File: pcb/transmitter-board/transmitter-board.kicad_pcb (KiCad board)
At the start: 2 copper layers, 28.9 x 20.5 mm, 28 parts, among them J1 USB-C_USB-310F-B-SU, Q3 AO3400A, Q4 AO3400A, SW1 SW_DPDT_x2, U1 NE555D, U3 TP4056-42-ESOP8, U4 DW01A

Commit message: Move USB
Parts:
- moved J1 1.05 mm to (161.3, 119.4)
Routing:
- net +3V8: track 35.4 -> 39.1 mm
- net GND: track 39.5 -> 38.1 mm
- net /IN+: track 41.0 -> 42.2 mm
- net Net-(J1-CC1): track 13.9 -> 12.7 mm
- net Net-(J1-CC2): track 6.40 -> 7.45 mm
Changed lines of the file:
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@@
 	(footprint "DW-footprints:USB-C-Receptacle_USB-310-B-SU"
 		(layer "F.Cu")
-		(at 161.33 118.375)
+		(at 161.33 119.425)
 		(descr "3A 1 Surface Mount, Right Angle 16P Female Type-C SMD USB Connectors ROHS")
 		(tags "USB, CONNECTOR, SMD")
@@
 	)
 	(segment
-		(start 157.585 114.695)
-		(end 157.01 115.27)
-		(width 0.2)
-		(layer "F.Cu")
-		(net 2)
-	)
-	(segment
 		(start 165.944222 113.237753)
 		(end 165.944222 112.854742)
@@
 	)
 	(segment
-		(start 158.13 114.695)
-		(end 157.585 114.695)
-		(width 0.2)
-		(layer "F.Cu")
-		(net 2)
-	)
-	(segment
 		(start 166.989903 110.181374)
 		(end 166.989903 111.659946)
@@
 	)
 	(segment
-		(start 163.73 114.695)
-		(end 163.73 115.083112)
+		(start 159.95 117.35)
+		(end 162.7 117.35)
 		(width 0.2)
 		(layer "F.Cu")
@@
 	)
 	(segment
-		(start 159.35 115.7)
-		(end 158.93 115.28)
+		(start 158.9 115.02)
+		(end 158.9 115.594999)
+		(width 0.2)
+		(layer "F.Cu")
+		(net 4)
+	)
+	(segment
+		(start 158.93 116.33)
+		(end 159.95 117.35)
 		(width 0.2)
 		(layer "F.Cu")
@@
 	)
 	(segment
-		(start 163.73 114.695)
-		(end 163.73 115.22)
+		(start 158.93 115.745)
+		(end 158.93 116.33)
 		(width 0.2)
 		(layer "F.Cu")
@@
 	)
 	(segment
-		(start 163.113112 115.7)
-		(end 159.35 115.7)
+		(start 163.4 116.683992)
+		(end 163.73 116.353992)
+		(width 0.2)
+		(layer "F.Cu")
+		(net 4)
+	)
+	(segment
+		(start 163.73 116.353992)
+		(end 163.73 115.745)
+		(width 0.2)
+		(layer "F.Cu")
+		(net 4)
+	)
+	(segment
+		(start 162.7 117.35)
+		(end 163.366008 116.683992)
 		(width 0.2)
 		(layer "F.Cu")
@@
 	)
 	(segment
-		(start 163.73 115.083112)
-		(end 163.113112 115.7)
-		(width 0.2)
+		(start 166.339634 109.22)
+		(end 165.727866 108.608232)
+		(width 0.3)
 		(layer "F.Cu")
 		(net 4)
 	)
 	(segment
-		(start 166.339634 109.22)
-		(end 165.727866 108.608232)
-		(width 0.3)
+		(start 163.366008 116.683992)
+		(end 163.4 116.683992)
+		(width 0.2)
 		(layer "F.Cu")
 		(net 4)
@@
 	)
 	(segment
+		(start 158.35 119.55)
+		(end 157.2 118.4)
+		(width 0.2)
+		(layer "B.Cu")
+		(net 6)
+	)
+	(segment
+		(start 150.772512 118.1)
+		(end 150.001364 117.328852)
+		(width 0.2)
+		(layer "B.Cu")
+		(net 6)
+	)
+	(segment
 		(start 165.73785 110.188892)
 		(end 166.610147 109.316594)
@@
 	)
 	(segment
-		(start 150.514534 116.815682)
-		(end 161.534318 116.815682)
+		(start 162.75 118.9)
+		(end 162.1 119.55)
 		(width 0.2)
 		(layer "B.Cu")
@@
 	)
 	(segment
-		(start 165.73785 112.61215)
-		(end 165.73785 110.188892)
+		(start 155.2 118.1)
+		(end 150.772512 118.1)
+		(width 0.2)
+		(layer "B.Cu")
+		(net 6)
+	)
+	(segment
+		(start 157.2 118.4)
+		(end 155.5 118.4)
+		(width 0.2)
+		(layer "B.Cu")
+		(net 6)
+	)
+	(segment
+		(start 155.5 118.4)
+		(end 155.2 118.1)
 		(width 0.2)
 		(layer "B.Cu")
@@
 	)
 	(segment
-		(start 150.001364 117.328852)
-		(end 150.514534 116.815682)
+		(start 162.75 116.65)
+		(end 162.75 118.9)
 		(width 0.2)
 		(layer "B.Cu")
@@
 	)
 	(segment
-		(start 161.534318 116.815682)
-		(end 165.73785 112.61215)
+		(start 162.1 119.55)
+		(end 158.35 119.55)
+		(width 0.2)
+		(layer "B.Cu")
+		(net 6)
+	)
+	(segment
+		(start 165.73785 110.188892)
+		(end 165.73785 113.66215)
+		(width 0.2)
+		(layer "B.Cu")
+		(net 6)
+	)
+	(segment
+		(start 165.73785 113.66215)
+		(end 162.75 116.65)
 		(width 0.2)
 		(layer "B.Cu")
@@
 	)
 	(segment
-		(start 166.156679 113.75)
-		(end 167.647066 115.240387)
+		(start 163.08 114.120001)
+		(end 163.08 115.745)
 		(width 0.15)
 		(layer "F.Cu")
@@
 	)
 	(segment
-		(start 163.08 114.695)
-		(end 163.08 114.120001)
+		(start 167.647066 115.240387)
+		(end 166.156679 113.75)
 		(width 0.15)
 		(layer "F.Cu")
@@
 	)
 	(segment
-		(start 167.647066 115.240387)
-		(end 167.647066 115.727887)
+		(start 166.156679 113.75)
+		(end 163.450001 113.75)
 		(width 0.15)
 		(layer "F.Cu")
@@
 	(segment
 		(start 163.450001 113.75)
-		(end 166.156679 113.75)
+		(end 163.08 114.120001)
 		(width 0.15)
 		(layer "F.Cu")
@@
 	)
 	(segment
-		(start 163.08 114.120001)
-		(end 163.450001 113.75)
+		(start 167.647066 115.727887)
+		(end 167.647066 115.240387)
 		(width 0.15)
 		(layer "F.Cu")
@@
 	)
 	(segment
+		(start 168.1 116.7)
+		(end 169.082846 115.717154)
+		(width 0.15)
+		(layer "F.Cu")
+		(net 31)
+	)
+	(segment
+		(start 167.4 117)
+		(end 167.7 116.7)
+		(width 0.15)
+		(layer "F.Cu")
+		(net 31)
+	)
+	(segment
+		(start 161.9 118.15)
+		(end 165.55 118.15)
+		(width 0.15)
+		(layer "F.Cu")
+		(net 31)
+	)
+	(segment
 		(start 169.082846 115.717154)
 		(end 169.439439 115.717154)
@@
 	)
 	(segment
-		(start 160.08 113.77)
-		(end 160.15 113.7)
+		(start 160.08 116.73)
+		(end 160.1 116.75)
 		(width 0.15)
 		(layer "F.Cu")
@@
 	)
 	(segment
-		(start 160.4 116.2)
-		(end 161.2 117)
+		(start 160.1 115.725001)
+		(end 160.08 115.745001)
 		(width 0.15)
 		(layer "F.Cu")
@@
 	)
 	(segment
-		(start 167.4 117)
-		(end 167.7 116.7)
+		(start 167.05 117)
+		(end 167.4 117)
 		(width 0.15)
 		(layer "F.Cu")
@@
 	)
 	(segment
-		(start 167.7 116.7)
-		(end 168.1 116.7)
+		(start 165.55 118.15)
+		(end 166.7 117)
 		(width 0.15)
 		(layer "F.Cu")
@@
 	)
 	(segment
-		(start 161.2 117)
-		(end 167.4 117)
+		(start 166.7 117)
+		(end 167.05 117)
 		(width 0.15)
 		(layer "F.Cu")
@@
 	)
 	(segment
-		(start 168.1 116.7)
-		(end 169.082846 115.717154)
+		(start 160.08 115.745001)
+		(end 160.08 115.52)
 		(width 0.15)
 		(layer "F.Cu")
@@
 	)
 	(segment
-		(start 160.08 114.695001)
-		(end 160.08 113.77)
+		(start 167.7 116.7)
+		(end 168.1 116.7)
+		(width 0.15)
+		(layer "F.Cu")
+		(net 31)
+	)
+	(segment
+		(start 160.08 115.745001)
+		(end 160.08 116.73)
+		(width 0.15)
+		(layer "F.Cu")
+		(net 31)
+	)
+	(segment
+		(start 160.08 115.52)
+		(end 160.1 115.5)
 		(width 0.15)
 		(layer "F.Cu")
@@
 		(net 31)
 	)
+	(segment
+		(start 160.1 116.75)
+		(end 160.15 116.8)
+		(width 0.15)
+		(layer "F.Cu")
+		(net 31)
+	)
 	(via
-		(at 160.4 116.2)
+		(at 160.1 116.75)
 		(size 0.5)
 		(drill 0.3)
@@
 	)
 	(via
-		(at 160.15 113.7)
+		(at 161.9 118.15)
 		(size 0.5)
 		(drill 0.3)
 		(layers "F.Cu" "B.Cu")
-		(free yes)
 		(net 31)
 	)
 	(segment
-		(start 160.15 115.95)
-		(end 160.4 116.2)
+		(start 160.1 116.75)
+		(end 161.5 118.15)
 		(width 0.15)
 		(layer "B.Cu")
@@
 	)
 	(segment
-		(start 160.15 113.7)
-		(end 160.15 115.95)
+		(start 161.5 118.15)
+		(end 161.9 118.15)
 		(width 0.15)
 		(layer "B.Cu")

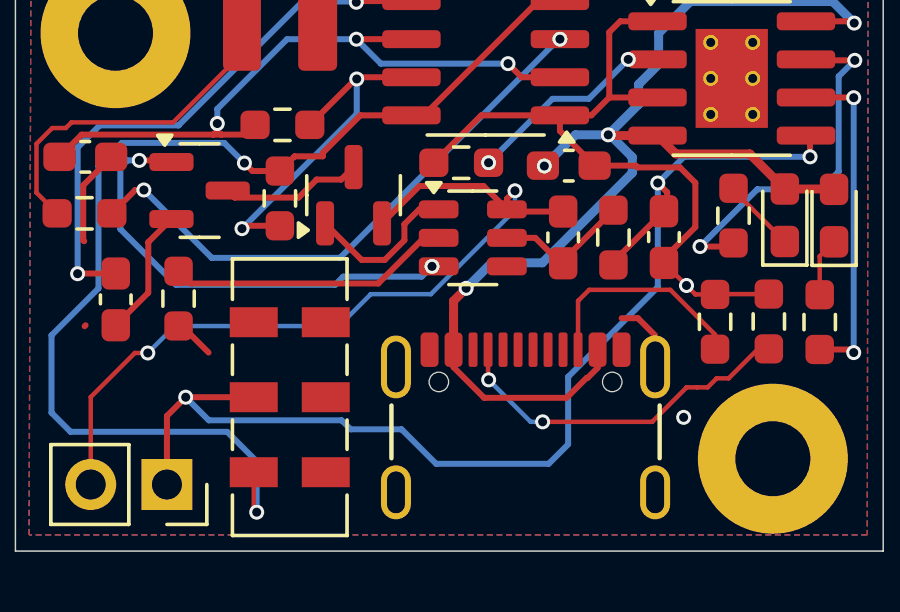
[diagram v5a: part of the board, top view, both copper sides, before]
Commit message: Edited transmitter-board schematic
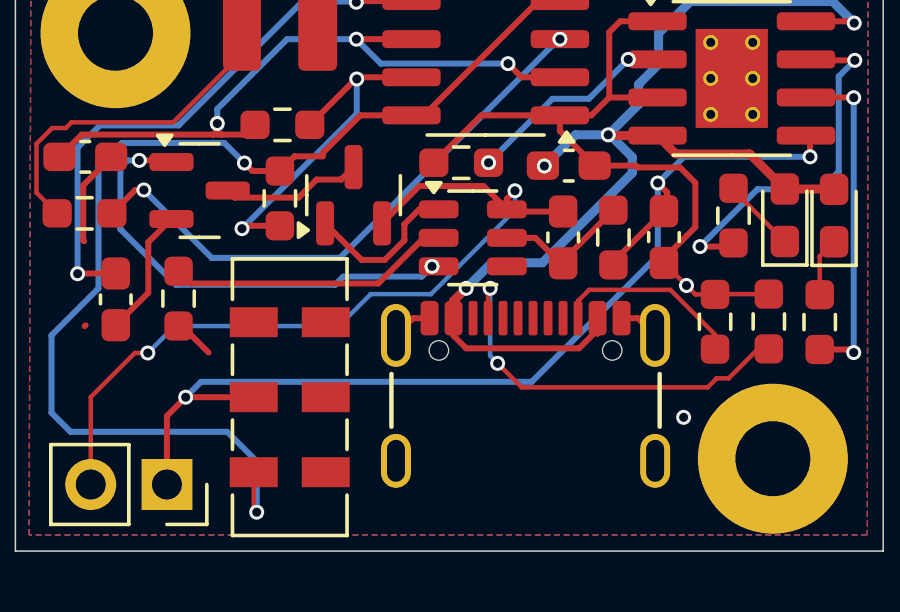
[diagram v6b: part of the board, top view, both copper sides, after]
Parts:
- moved J1 1.05 mm to (161.3, 118.4)
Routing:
- net +3V8: track 39.1 -> 35.4 mm
- net GND: track 38.1 -> 39.5 mm
- net /IN+: track 42.2 -> 41.0 mm
- net Net-(J1-CC1): track 12.7 -> 13.9 mm
- net Net-(J1-CC2): track 7.45 -> 6.40 mm
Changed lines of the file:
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@@
 	(footprint "DW-footprints:USB-C-Receptacle_USB-310-B-SU"
 		(layer "F.Cu")
-		(at 161.33 119.425)
+		(at 161.33 118.375)
 		(descr "3A 1 Surface Mount, Right Angle 16P Female Type-C SMD USB Connectors ROHS")
 		(tags "USB, CONNECTOR, SMD")
@@
 	)
 	(segment
+		(start 157.585 114.695)
+		(end 157.01 115.27)
+		(width 0.2)
+		(layer "F.Cu")
+		(net 2)
+	)
+	(segment
 		(start 165.944222 113.237753)
 		(end 165.944222 112.854742)
@@
 	)
 	(segment
+		(start 158.13 114.695)
+		(end 157.585 114.695)
+		(width 0.2)
+		(layer "F.Cu")
+		(net 2)
+	)
+	(segment
 		(start 166.989903 110.181374)
 		(end 166.989903 111.659946)
@@
 	)
 	(segment
-		(start 159.95 117.35)
-		(end 162.7 117.35)
+		(start 163.73 114.695)
+		(end 163.73 115.083112)
 		(width 0.2)
 		(layer "F.Cu")
@@
 	)
 	(segment
-		(start 158.9 115.02)
-		(end 158.9 115.594999)
-		(width 0.2)
-		(layer "F.Cu")
-		(net 4)
-	)
-	(segment
-		(start 158.93 116.33)
-		(end 159.95 117.35)
+		(start 159.35 115.7)
+		(end 158.93 115.28)
 		(width 0.2)
 		(layer "F.Cu")
@@
 	)
 	(segment
-		(start 158.93 115.745)
-		(end 158.93 116.33)
+		(start 163.73 114.695)
+		(end 163.73 115.22)
 		(width 0.2)
 		(layer "F.Cu")
@@
 	)
 	(segment
-		(start 163.4 116.683992)
-		(end 163.73 116.353992)
-		(width 0.2)
-		(layer "F.Cu")
-		(net 4)
-	)
-	(segment
-		(start 163.73 116.353992)
-		(end 163.73 115.745)
-		(width 0.2)
-		(layer "F.Cu")
-		(net 4)
-	)
-	(segment
-		(start 162.7 117.35)
-		(end 163.366008 116.683992)
+		(start 163.113112 115.7)
+		(end 159.35 115.7)
 		(width 0.2)
 		(layer "F.Cu")
@@
 	)
 	(segment
-		(start 166.339634 109.22)
-		(end 165.727866 108.608232)
-		(width 0.3)
+		(start 163.73 115.083112)
+		(end 163.113112 115.7)
+		(width 0.2)
 		(layer "F.Cu")
 		(net 4)
 	)
 	(segment
-		(start 163.366008 116.683992)
-		(end 163.4 116.683992)
-		(width 0.2)
+		(start 166.339634 109.22)
+		(end 165.727866 108.608232)
+		(width 0.3)
 		(layer "F.Cu")
 		(net 4)
@@
 	)
 	(segment
-		(start 158.35 119.55)
-		(end 157.2 118.4)
-		(width 0.2)
-		(layer "B.Cu")
-		(net 6)
-	)
-	(segment
-		(start 150.772512 118.1)
-		(end 150.001364 117.328852)
-		(width 0.2)
-		(layer "B.Cu")
-		(net 6)
-	)
-	(segment
 		(start 165.73785 110.188892)
 		(end 166.610147 109.316594)
@@
 	)
 	(segment
-		(start 162.75 118.9)
-		(end 162.1 119.55)
+		(start 150.514534 116.815682)
+		(end 161.534318 116.815682)
 		(width 0.2)
 		(layer "B.Cu")
@@
 	)
 	(segment
-		(start 155.2 118.1)
-		(end 150.772512 118.1)
-		(width 0.2)
-		(layer "B.Cu")
-		(net 6)
-	)
-	(segment
-		(start 157.2 118.4)
-		(end 155.5 118.4)
-		(width 0.2)
-		(layer "B.Cu")
-		(net 6)
-	)
-	(segment
-		(start 155.5 118.4)
-		(end 155.2 118.1)
+		(start 165.73785 112.61215)
+		(end 165.73785 110.188892)
 		(width 0.2)
 		(layer "B.Cu")
@@
 	)
 	(segment
-		(start 162.75 116.65)
-		(end 162.75 118.9)
-		(width 0.2)
-		(layer "B.Cu")
-		(net 6)
-	)
-	(segment
-		(start 162.1 119.55)
-		(end 158.35 119.55)
-		(width 0.2)
-		(layer "B.Cu")
-		(net 6)
-	)
-	(segment
-		(start 165.73785 110.188892)
-		(end 165.73785 113.66215)
+		(start 150.001364 117.328852)
+		(end 150.514534 116.815682)
 		(width 0.2)
 		(layer "B.Cu")
@@
 	)
 	(segment
-		(start 165.73785 113.66215)
-		(end 162.75 116.65)
+		(start 161.534318 116.815682)
+		(end 165.73785 112.61215)
 		(width 0.2)
 		(layer "B.Cu")
@@
 	)
 	(segment
-		(start 163.08 114.120001)
-		(end 163.08 115.745)
+		(start 166.156679 113.75)
+		(end 167.647066 115.240387)
 		(width 0.15)
 		(layer "F.Cu")
@@
 	)
 	(segment
-		(start 167.647066 115.240387)
-		(end 166.156679 113.75)
+		(start 163.08 114.695)
+		(end 163.08 114.120001)
 		(width 0.15)
 		(layer "F.Cu")
@@
 	)
 	(segment
-		(start 166.156679 113.75)
-		(end 163.450001 113.75)
+		(start 167.647066 115.240387)
+		(end 167.647066 115.727887)
 		(width 0.15)
 		(layer "F.Cu")
@@
 	(segment
 		(start 163.450001 113.75)
-		(end 163.08 114.120001)
+		(end 166.156679 113.75)
 		(width 0.15)
 		(layer "F.Cu")
@@
 	)
 	(segment
-		(start 167.647066 115.727887)
-		(end 167.647066 115.240387)
+		(start 163.08 114.120001)
+		(end 163.450001 113.75)
 		(width 0.15)
 		(layer "F.Cu")
@@
 	)
 	(segment
-		(start 168.1 116.7)
-		(end 169.082846 115.717154)
-		(width 0.15)
-		(layer "F.Cu")
-		(net 31)
-	)
-	(segment
-		(start 167.4 117)
-		(end 167.7 116.7)
-		(width 0.15)
-		(layer "F.Cu")
-		(net 31)
-	)
-	(segment
-		(start 161.9 118.15)
-		(end 165.55 118.15)
-		(width 0.15)
-		(layer "F.Cu")
-		(net 31)
-	)
-	(segment
 		(start 169.082846 115.717154)
 		(end 169.439439 115.717154)
@@
 	)
 	(segment
-		(start 160.08 116.73)
-		(end 160.1 116.75)
-		(width 0.15)
-		(layer "F.Cu")
-		(net 31)
-	)
-	(segment
-		(start 160.1 115.725001)
-		(end 160.08 115.745001)
-		(width 0.15)
-		(layer "F.Cu")
-		(net 31)
-	)
-	(segment
-		(start 167.05 117)
-		(end 167.4 117)
+		(start 160.08 113.77)
+		(end 160.15 113.7)
 		(width 0.15)
 		(layer "F.Cu")
@@
 	)
 	(segment
-		(start 165.55 118.15)
-		(end 166.7 117)
+		(start 160.4 116.2)
+		(end 161.2 117)
 		(width 0.15)
 		(layer "F.Cu")
@@
 	)
 	(segment
-		(start 166.7 117)
-		(end 167.05 117)
-		(width 0.15)
-		(layer "F.Cu")
-		(net 31)
-	)
-	(segment
-		(start 160.08 115.745001)
-		(end 160.08 115.52)
+		(start 167.4 117)
+		(end 167.7 116.7)
 		(width 0.15)
 		(layer "F.Cu")
@@
 	)
 	(segment
-		(start 160.08 115.745001)
-		(end 160.08 116.73)
+		(start 161.2 117)
+		(end 167.4 117)
 		(width 0.15)
 		(layer "F.Cu")
@@
 	)
 	(segment
-		(start 160.08 115.52)
-		(end 160.1 115.5)
+		(start 168.1 116.7)
+		(end 169.082846 115.717154)
 		(width 0.15)
 		(layer "F.Cu")
@@
 	)
 	(segment
-		(start 169.439439 115.717154)
-		(end 169.05263 115.717154)
+		(start 160.08 114.695001)
+		(end 160.08 113.77)
 		(width 0.15)
 		(layer "F.Cu")
@@
 	)
 	(segment
-		(start 160.1 116.75)
-		(end 160.15 116.8)
+		(start 169.439439 115.717154)
+		(end 169.05263 115.717154)
 		(width 0.15)
 		(layer "F.Cu")
@@
 	)
 	(via
-		(at 160.1 116.75)
+		(at 160.4 116.2)
 		(size 0.5)
 		(drill 0.3)
@@
 	)
 	(via
-		(at 161.9 118.15)
+		(at 160.15 113.7)
 		(size 0.5)
 		(drill 0.3)
 		(layers "F.Cu" "B.Cu")
+		(free yes)
 		(net 31)
 	)
 	(segment
-		(start 160.1 116.75)
-		(end 161.5 118.15)
+		(start 160.15 115.95)
+		(end 160.4 116.2)
 		(width 0.15)
 		(layer "B.Cu")
@@
 	)
 	(segment
-		(start 161.5 118.15)
-		(end 161.9 118.15)
+		(start 160.15 113.7)
+		(end 160.15 115.95)
 		(width 0.15)
 		(layer "B.Cu")

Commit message: Clear ERC and DRC
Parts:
- D1: value R LED -> RED
- D2: value B LED -> BLUE
- D3: value IR LED -> IR
- R5: value 1.2k -> 10k
- R8: value 150 -> 200R
- U3: value TP4056-42-ESOP8 -> TP4056
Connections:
- net +3V8 renamed Net-(BT1-+)
- net /555OUT renamed Net-(U1-Q)
- net /B- renamed Net-(BT1--)
- net /IN+ renamed VBUS
